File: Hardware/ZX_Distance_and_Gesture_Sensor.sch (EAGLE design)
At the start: 47 parts, among them Q1 MMBT2222A, Q2 MOSFET-NCHANNEL2N7002PW, U1 BRM-2508VERT

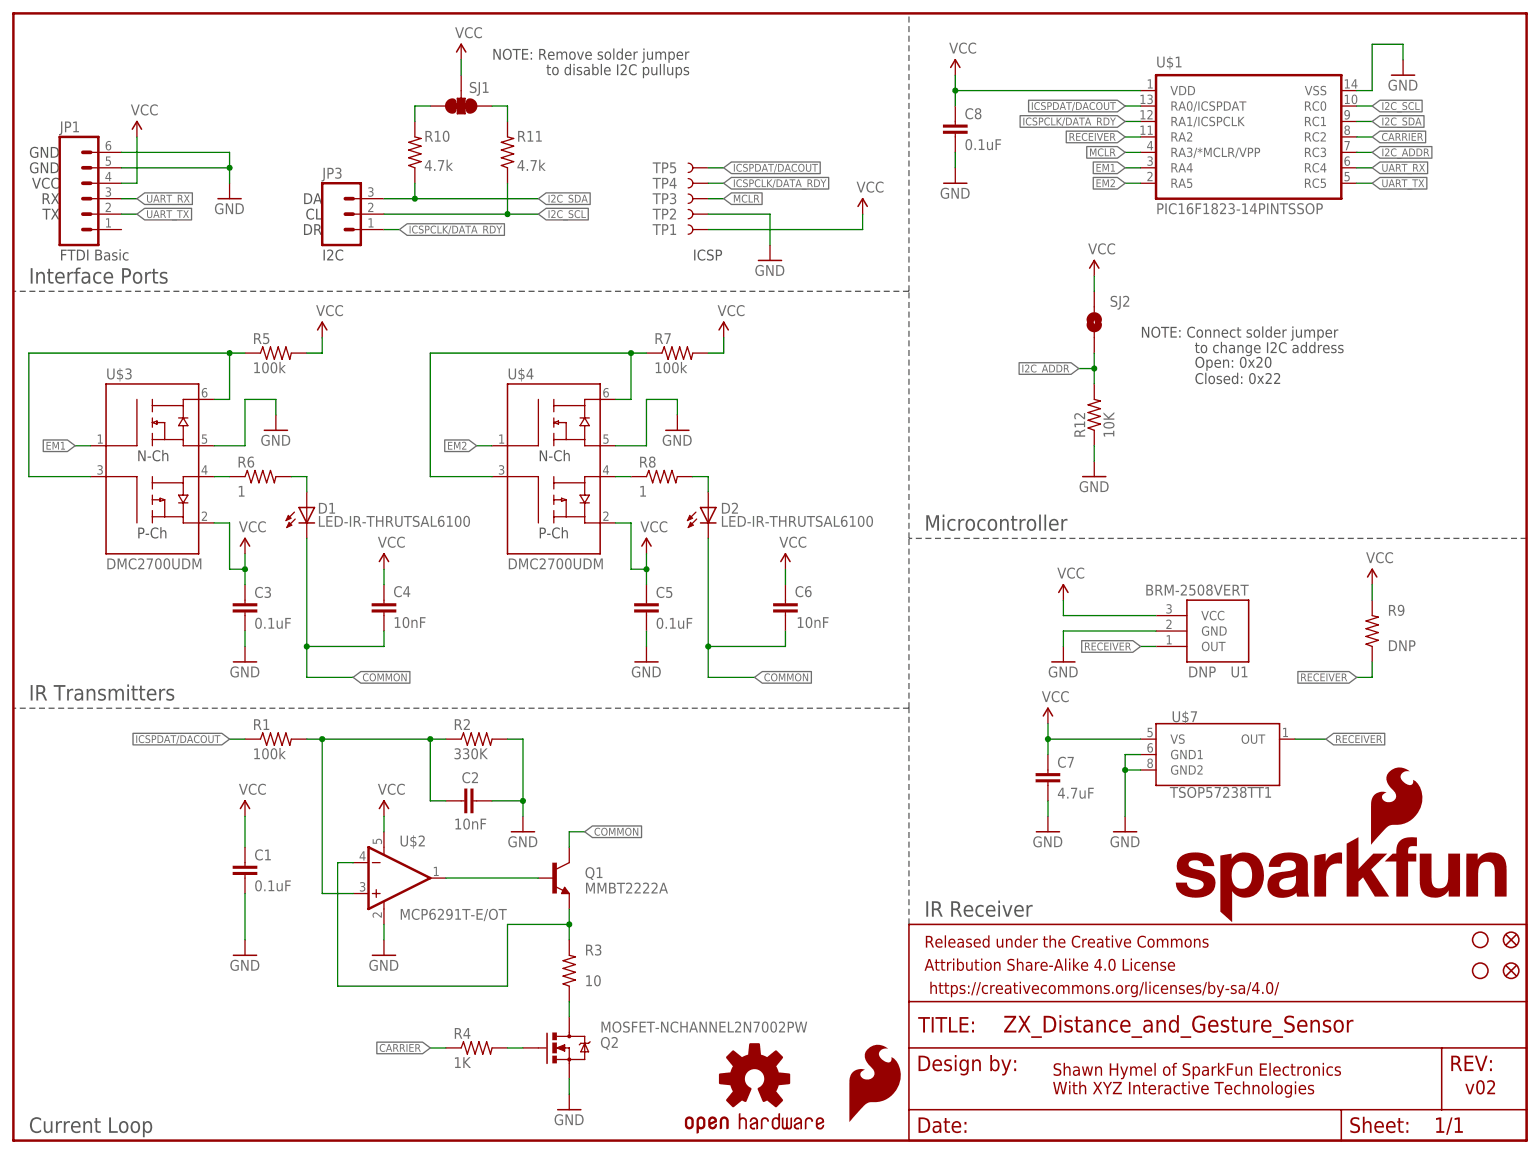
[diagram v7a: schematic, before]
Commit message: Added silk pinout. Ready for v02 review.
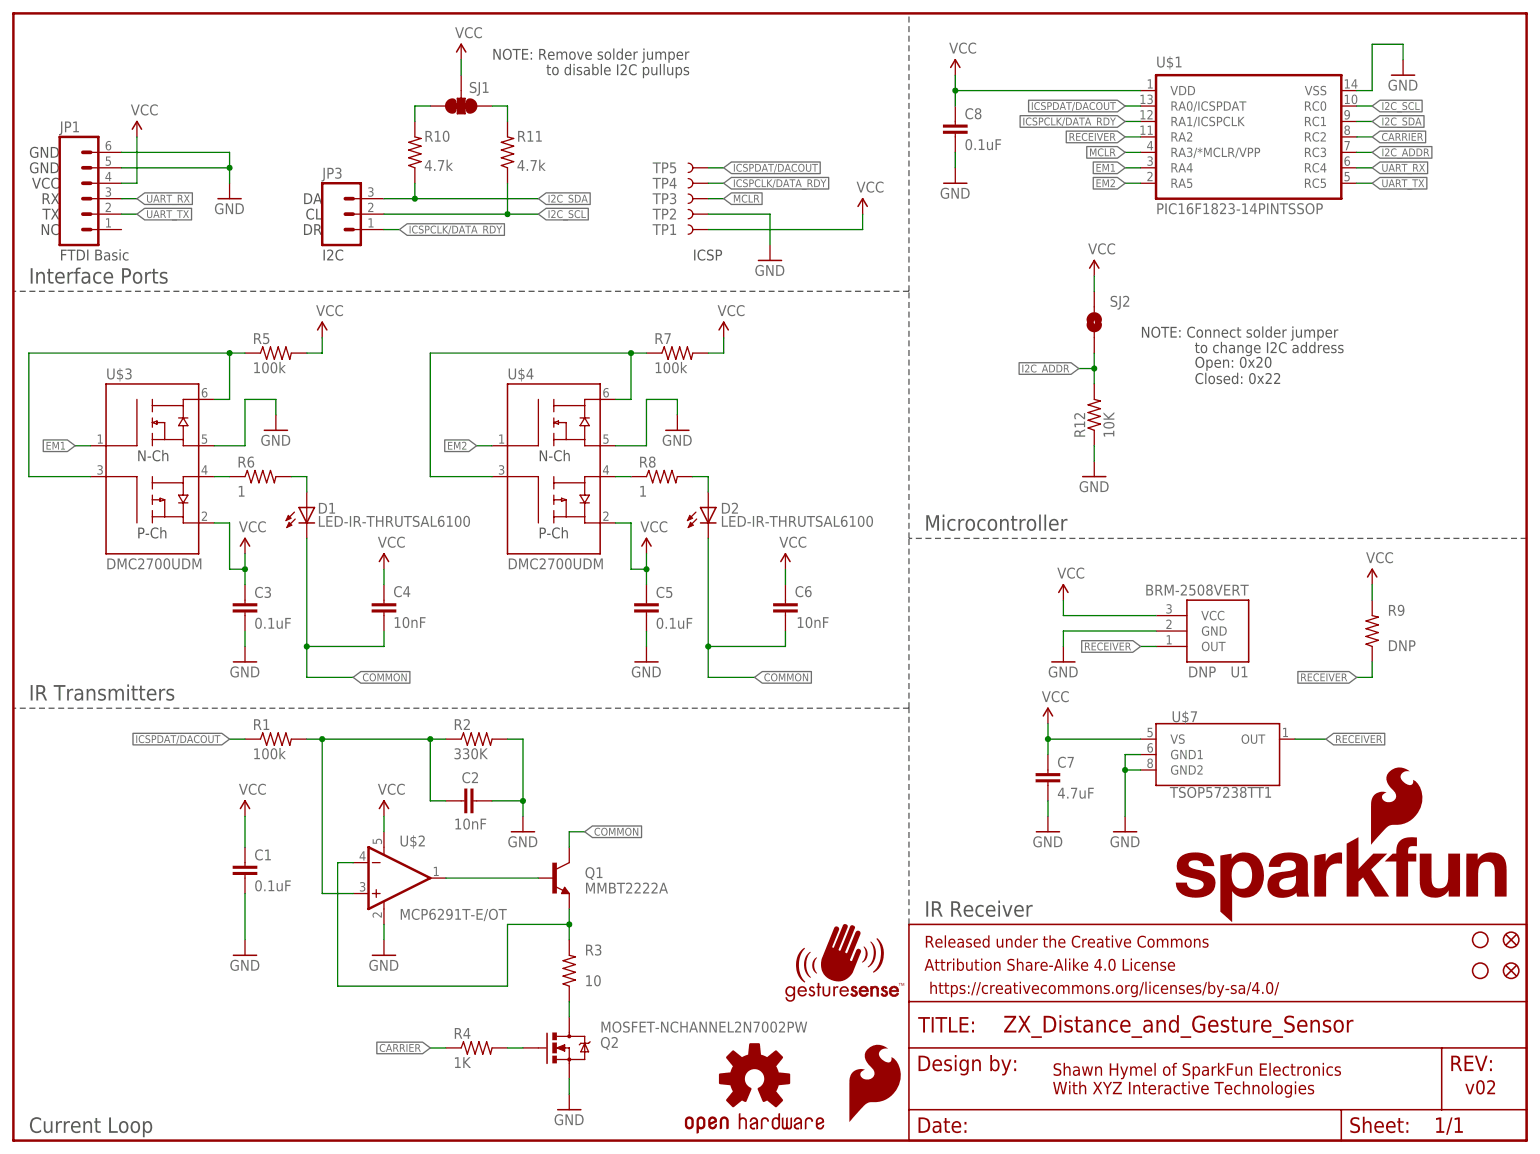
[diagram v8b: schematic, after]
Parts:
- added U$6: GESTURESENSE_LOGOSTEXT, SparkFun-Aesthetics:GESTURESENSE_LOGOSTEXT
- JP1: device SparkFun-Connectors:M06SIP -> SparkFun-Connectors:M06NO_SILK
- JP3: device SparkFun-Connectors:M03PTH -> SparkFun-Connectors:M031X03_NO_SILK
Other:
- note added: "NC"
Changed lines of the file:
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@@
 <part name="U$4" library="SparkFun-DiscreteSemi" deviceset="DMC2700UDM" device=""/>
 <part name="U$7" library="SparkFun-Sensors" deviceset="TSOP57238TT1" device=""/>
-<part name="JP1" library="SparkFun-Connectors" deviceset="M06" device="SIP"/>
-<part name="JP3" library="SparkFun-Connectors" deviceset="M03" device="PTH"/>
+<part name="JP1" library="SparkFun-Connectors" deviceset="M06" device="NO_SILK"/>
+<part name="JP3" library="SparkFun-Connectors" deviceset="M03" device="1X03_NO_SILK"/>
 <part name="GND1" library="SparkFun-Aesthetics" deviceset="GND" device=""/>
 <part name="SUPPLY1" library="SparkFun-Aesthetics" deviceset="VCC" device=""/>
@@
 <part name="SUPPLY16" library="SparkFun-Aesthetics" deviceset="VCC" device=""/>
 <part name="GND16" library="SparkFun-Aesthetics" deviceset="GND" device=""/>
+<part name="U$6" library="SparkFun-Aesthetics" deviceset="GESTURESENSE_LOGOS" device="TEXT"/>
 </parts>
 <sheets>
@@
 <text x="50.8" y="152.4" size="1.778" layer="97" align="center-right">CL</text>
 <text x="50.8" y="149.86" size="1.778" layer="97" align="center-right">DR</text>
+<text x="7.62" y="149.86" size="1.778" layer="97" align="center-right">NC</text>
 </plain>
 <instances>
@@
 <instance part="SUPPLY16" gate="G$1" x="172.72" y="88.9"/>
 <instance part="GND16" gate="1" x="172.72" y="78.74"/>
+<instance part="U$6" gate="G$1" x="127" y="22.86"/>
 </instances>
 <busses>
